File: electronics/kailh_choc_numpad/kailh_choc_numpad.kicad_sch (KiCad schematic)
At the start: 83 parts

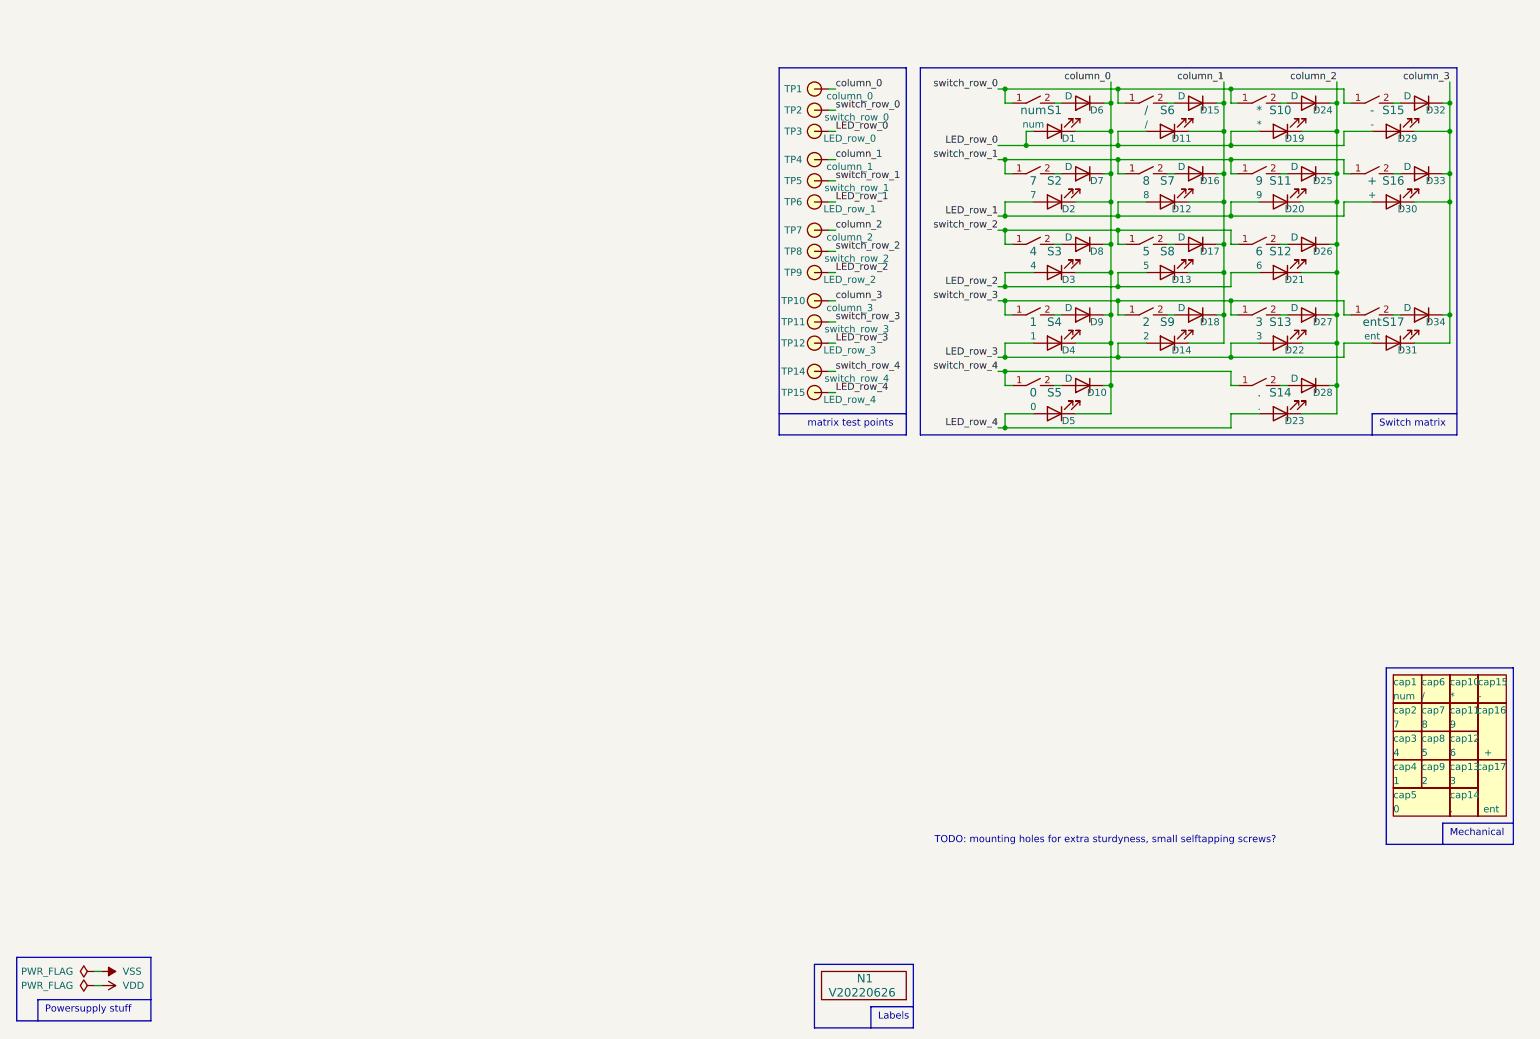
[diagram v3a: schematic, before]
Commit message: added, placed and routed ESD diodes
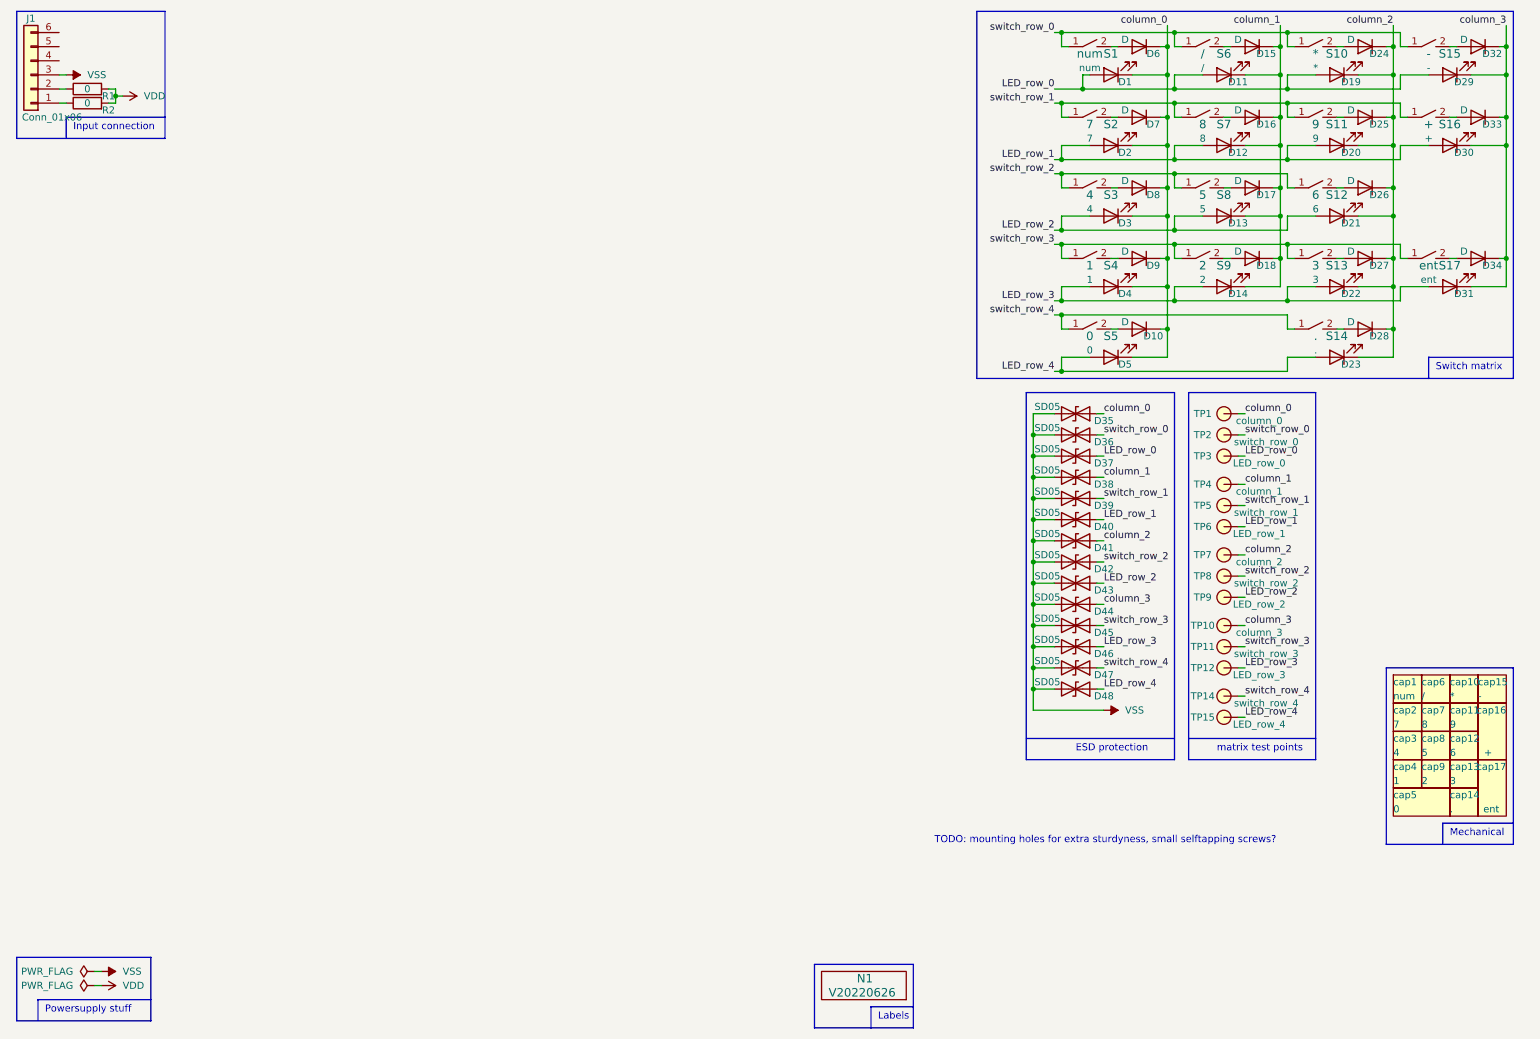
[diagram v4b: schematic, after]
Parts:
- added D35, D36, D37, D38, D39, D40, D41, D42, D43, D44, D45, D46, D47, D48: SD05, Diode_SMD:D_SOD-323, symbol Device:D_TVS
- added J1: Conn_01x06, Connector_JST:JST_PH_S6B-PH-K_1x06_P2.00mm_Horizontal, symbol Connector_Generic:Conn_01x06
- added R1, R2: 0, SquantorRcl:R_0603_hand, symbol Device:R
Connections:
- net LED_row_0: now also D37.1 (A1)
- net LED_row_1: now also D40.1 (A1)
- net LED_row_2: now also D43.1 (A1)
- net LED_row_3: now also D46.1 (A1)
- net LED_row_4: now also D48.1 (A1)
- net VDD: now also R1.2, R2.2
- net VSS: now also D35.2 (A2), D36.2 (A2), D37.2 (A2), D38.2 (A2), D39.2 (A2), D40.2 (A2), D41.2 (A2), D42.2 (A2), D43.2 (A2), D44.2 (A2), D45.2 (A2), D46.2 (A2), D47.2 (A2), D48.2 (A2), J1.3 (Pin_3)
- net column_0: now also D35.1 (A1)
- net column_1: now also D38.1 (A1)
- net column_2: now also D41.1 (A1)
- net column_3: now also D44.1 (A1)
- net switch_row_0: now also D36.1 (A1)
- net switch_row_1: now also D39.1 (A1)
- net switch_row_2: now also D42.1 (A1)
- net switch_row_3: now also D45.1 (A1)
- net switch_row_4: now also D47.1 (A1)
- new net: J1.2 (Pin_2), R1.1
- new net: J1.1 (Pin_1), R2.1
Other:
- note added: "ESD protection"
- note added: "Input connection"
- moved on the sheet: D1, D10, D11, D12, D13, D14, D15, D16, D17, D18, D19, D2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

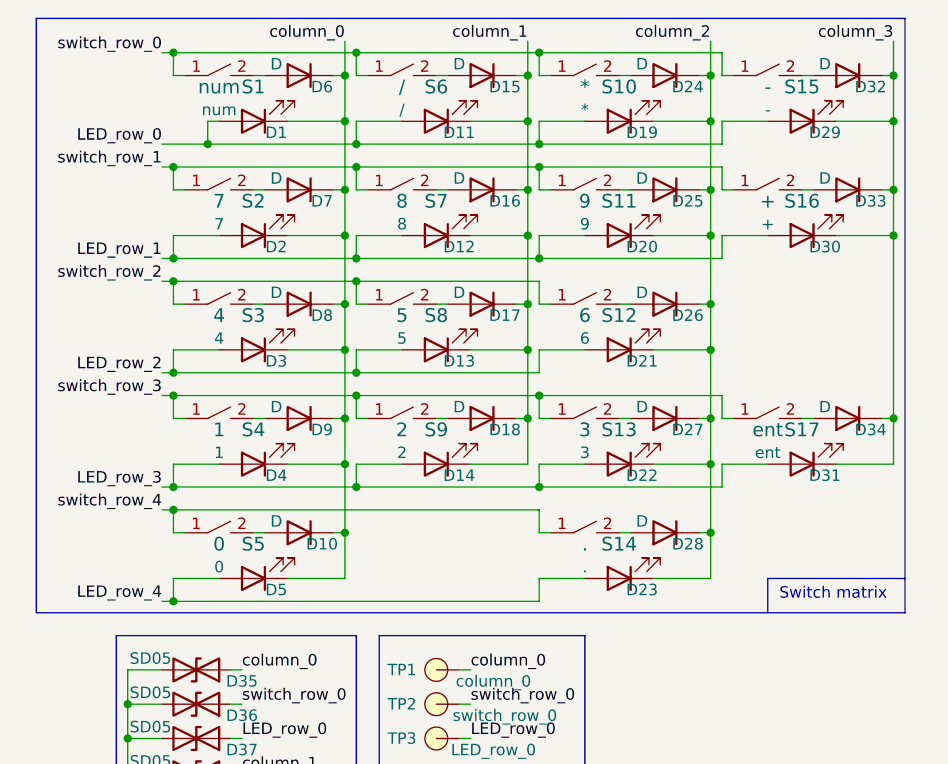
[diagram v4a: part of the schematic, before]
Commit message: added LED resistors
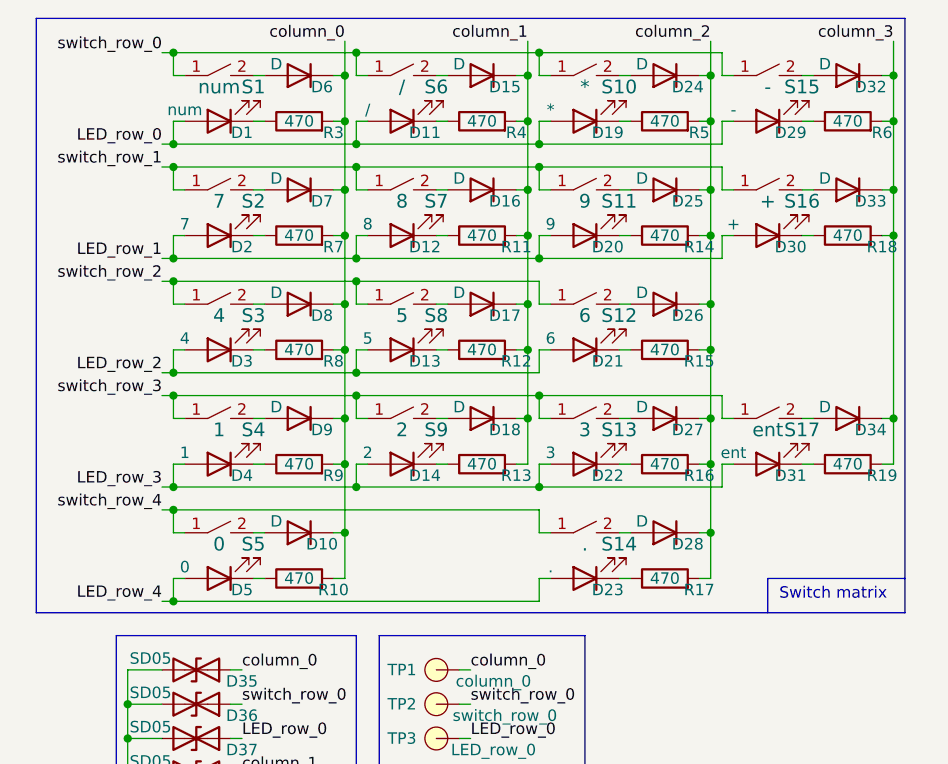
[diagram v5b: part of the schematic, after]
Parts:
- added R10, R11, R12, R13, R14, R15, R16, R17, R18, R19, R3, R4, R5, R6, R7, R8, R9: 470, SquantorRcl:R_0603_hand, symbol Device:R
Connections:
- net column_0: now also R10.2, R3.2, R7.2, R8.2, R9.2; no longer D1.1 (K), D2.1 (K), D3.1 (K), D4.1 (K), D5.1 (K)
- net column_1: now also R11.2, R12.2, R13.2, R4.2; no longer D11.1 (K), D12.1 (K), D13.1 (K), D14.1 (K)
- net column_2: now also R14.2, R15.2, R16.2, R17.2, R5.2; no longer D19.1 (K), D20.1 (K), D21.1 (K), D22.1 (K), D23.1 (K)
- net column_3: now also R18.2, R19.2, R6.2; no longer D29.1 (K), D30.1 (K), D31.1 (K)
- new net: D1.1 (K), R3.1
- new net: D13.1 (K), R12.1
- new net: D21.1 (K), R15.1
- new net: D3.1 (K), R8.1
- new net: D30.1 (K), R18.1
- new net: D12.1 (K), R11.1
- new net: D23.1 (K), R17.1
- new net: D2.1 (K), R7.1
- new net: D19.1 (K), R5.1
- new net: D20.1 (K), R14.1
- new net: D22.1 (K), R16.1
- new net: D5.1 (K), R10.1
- new net: D31.1 (K), R19.1
- new net: D11.1 (K), R4.1
- new net: D29.1 (K), R6.1
- new net: D14.1 (K), R13.1
- new net: D4.1 (K), R9.1
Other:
- moved on the sheet: D1, D11, D12, D13, D14, D19, D2, D20, D21, D22, D23, D29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

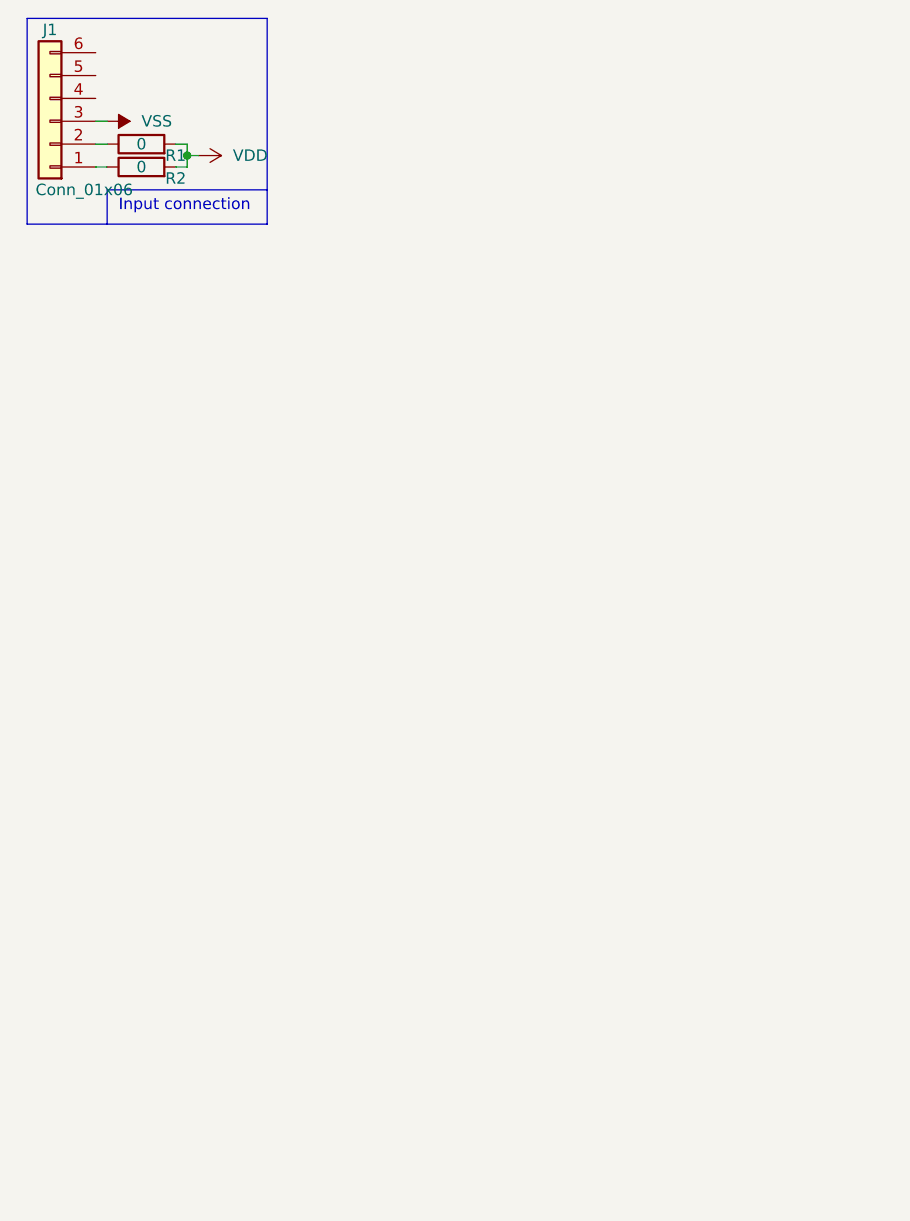
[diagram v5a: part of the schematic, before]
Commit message: added i2c port expander but wrong footprint, now
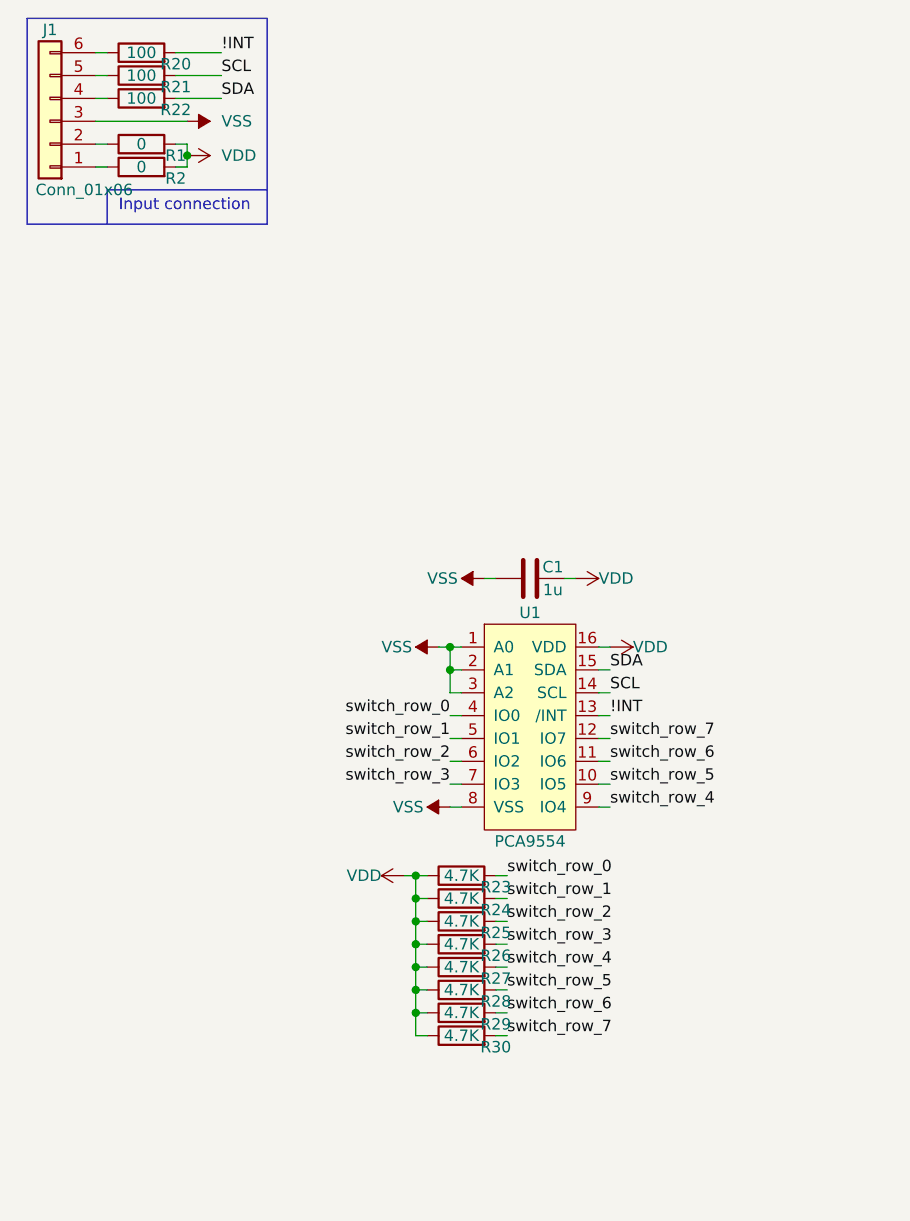
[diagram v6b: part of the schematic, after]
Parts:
- added C1: 1u, SquantorRcl:C_0603, symbol Device:C
- added R20, R21, R22: 100, SquantorRcl:R_0603_hand, symbol Device:R
- added R23, R24, R25, R26, R27, R28, R29, R30: 4.7K, SquantorRcl:R_0603_hand, symbol Device:R
- added U1: PCA9554, SquantorIC:SOT162-1-NXP, symbol SquantorNxp:PCA9554
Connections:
- net VDD: now also C1.2, R23.1, R24.1, R25.1, R26.1, R27.1, R28.1, R29.1, R30.1, U1.16 (VDD)
- net VSS: now also C1.1, U1.1 (A0), U1.2 (A1), U1.3 (A2), U1.8 (VSS)
- net switch_row_0: now also R23.2, U1.4 (IO0)
- net switch_row_1: now also R24.2, U1.5 (IO1)
- net switch_row_2: now also R25.2, U1.6 (IO2)
- net switch_row_3: now also R26.2, U1.7 (IO3)
- net switch_row_4: now also R27.2, U1.9 (IO4)
- net at J1.4 (Pin_4): now also R22.1
- net at J1.5 (Pin_5): now also R21.1
- net at J1.6 (Pin_6): now also R20.1
- new net !INT: R20.2, U1.13 (/INT)
- new net SCL: R21.2, U1.14 (SCL)
- new net SDA: R22.2, U1.15 (SDA)
- new net switch_row_5: R28.2, U1.10 (IO5)
- new net switch_row_6: R29.2, U1.11 (IO6)
- new net switch_row_7: R30.2, U1.12 (IO7)

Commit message: added I2C port expanders
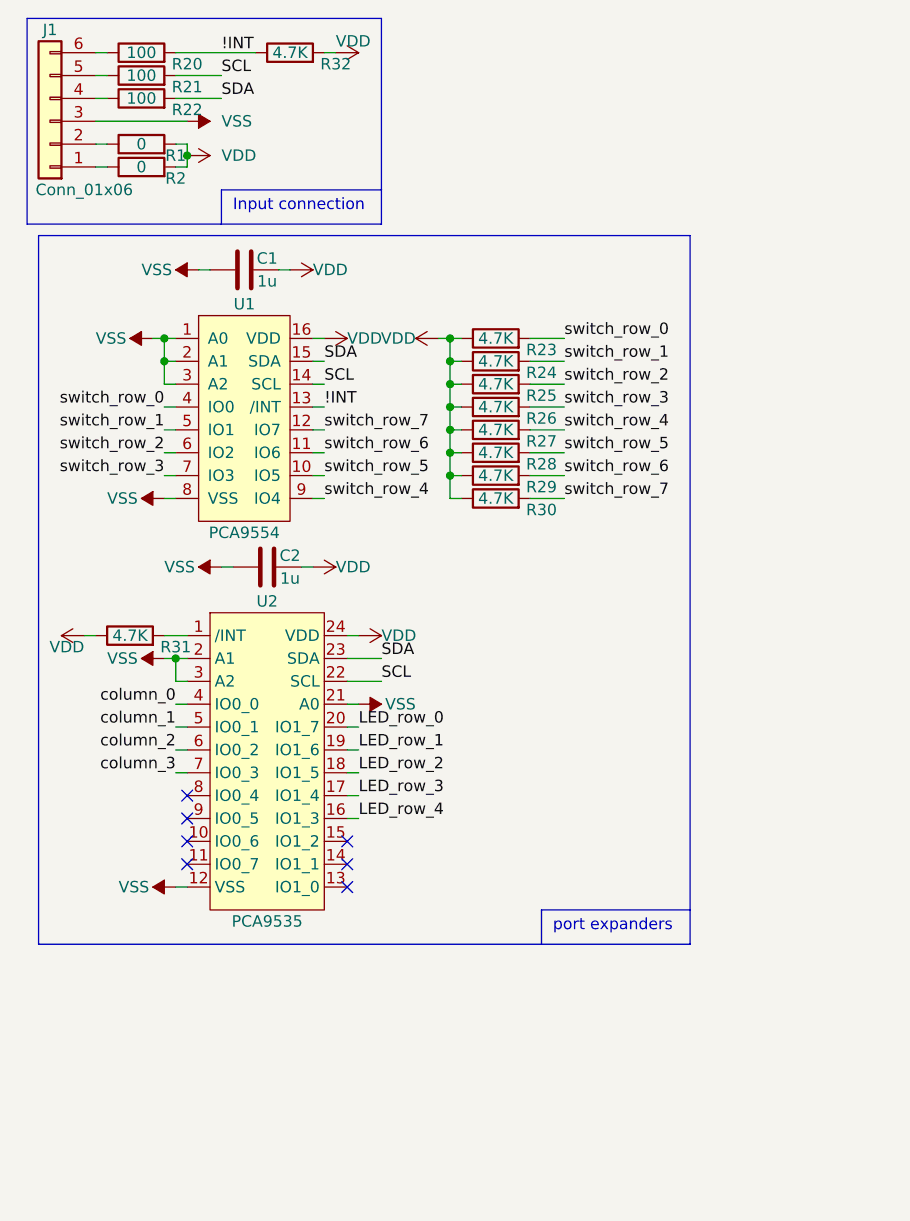
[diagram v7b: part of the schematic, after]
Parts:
- added C2: 1u, SquantorRcl:C_0603, symbol Device:C
- added R31, R32: 4.7K, SquantorRcl:R_0603_hand, symbol Device:R
- added U2: PCA9535, SquantorIC:SOT355-1-NXP, symbol SquantorNxp:PCA9535
- U1: footprint SquantorIC:SOT162-1-NXP -> SquantorIC:SOT403-1-NXP
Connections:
- net !INT: now also R32.1
- net LED_row_0: now also U2.20 (IO1_7)
- net LED_row_1: now also U2.19 (IO1_6)
- net LED_row_2: now also U2.18 (IO1_5)
- net LED_row_3: now also U2.17 (IO1_4)
- net LED_row_4: now also U2.16 (IO1_3)
- net SCL: now also U2.22 (SCL)
- net SDA: now also U2.23 (SDA)
- net VDD: now also C2.2, R31.1, R32.2, U2.24 (VDD)
- net VSS: now also C2.1, U2.12 (VSS), U2.2 (A1), U2.21 (A0), U2.3 (A2)
- net column_0: now also U2.4 (IO0_0)
- net column_1: now also U2.5 (IO0_1)
- net column_2: now also U2.6 (IO0_2)
- net column_3: now also U2.7 (IO0_3)
- new net: R31.2, U2.1 (/INT)
- no-connect marks 0 -> 7
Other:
- note added: "port expanders"
- moved on the sheet: C1, R23, R24, R25, R26, R27, R28, R29, R30, U1
